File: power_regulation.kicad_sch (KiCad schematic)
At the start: 122 parts, among them IC3 NCV8184DR2G, IC4 MIE1W0505BGLVH-3R-P, J10 Conn_01x02_Pin, J7 V_bat_secondary, J8 Conn_01x02_Pin, J9 Conn_01x02_Pin, U10 OPA2387DR, U11 TPS7A2055PDBVR, U12 AP7361C-33Y5-13, U13 TPS7A2050PDBVR, U14 TPS7A2033PDBVR, U15 TPS7A2018PDBVRG4, U16 TLV75733PDYDR, U17 TPS7A2050PDBVR, U18 TPS7A2050PDBVR, U19 TPS7A2033PDBVR, U20 TPS7A2045PDBVR, U7 MCP1502T-50E/CHY, U8 TPS62933, U9 TPS62933

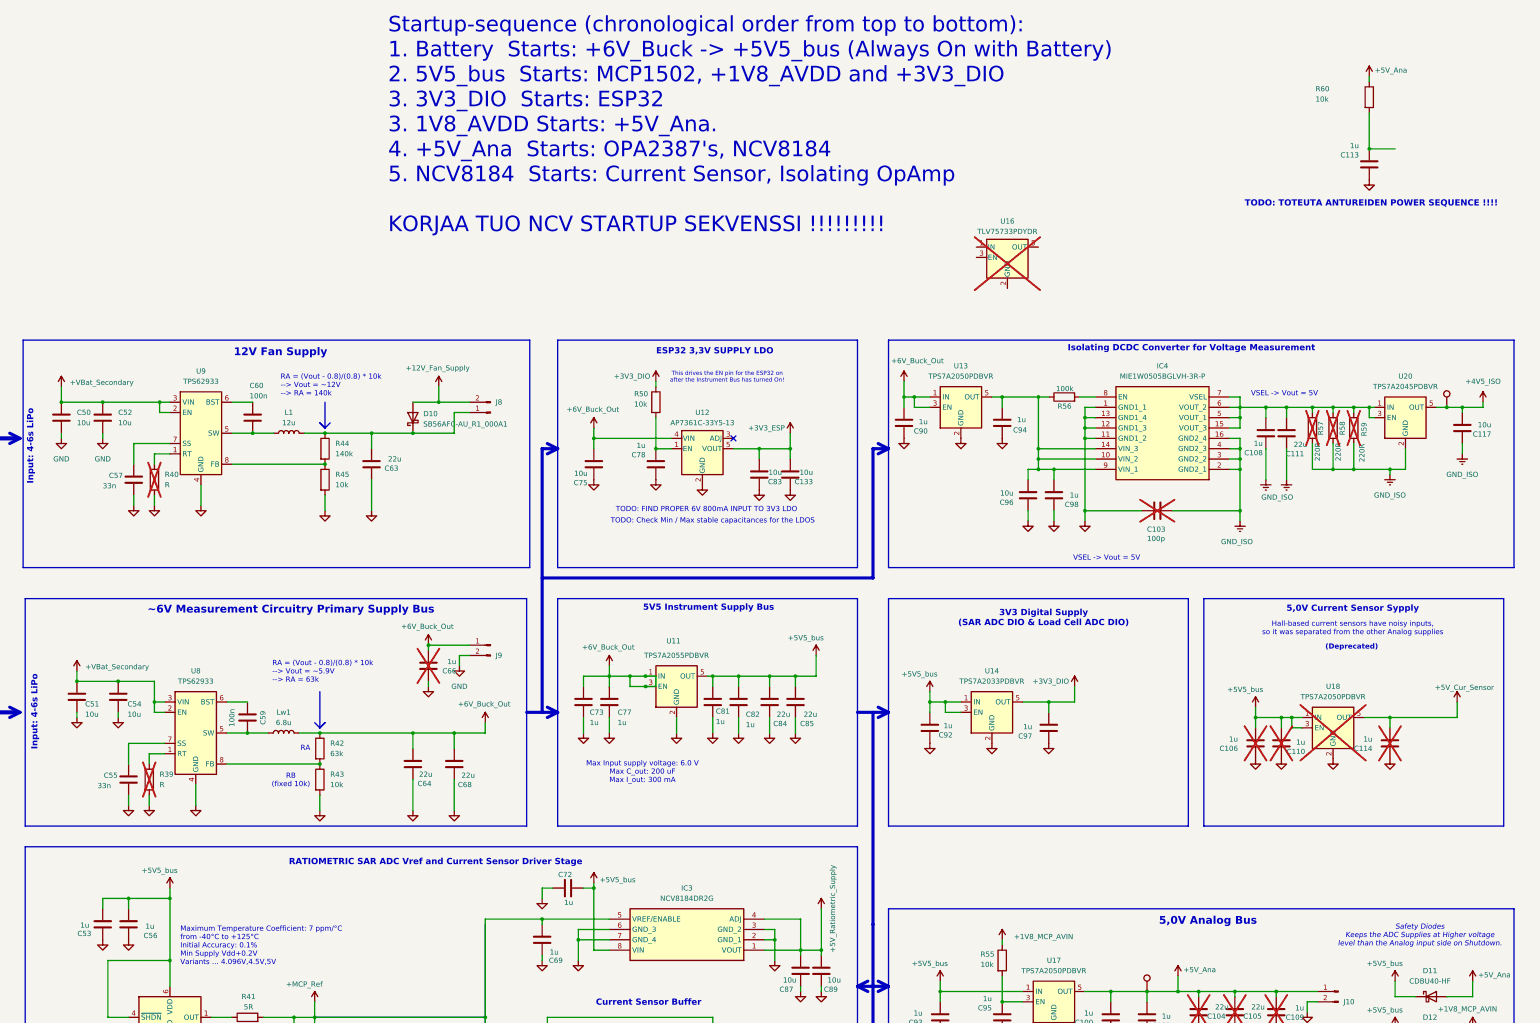
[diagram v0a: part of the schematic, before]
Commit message: Add LDO / Power sequencing for sensors
[KiCad Version: 10.0.3]
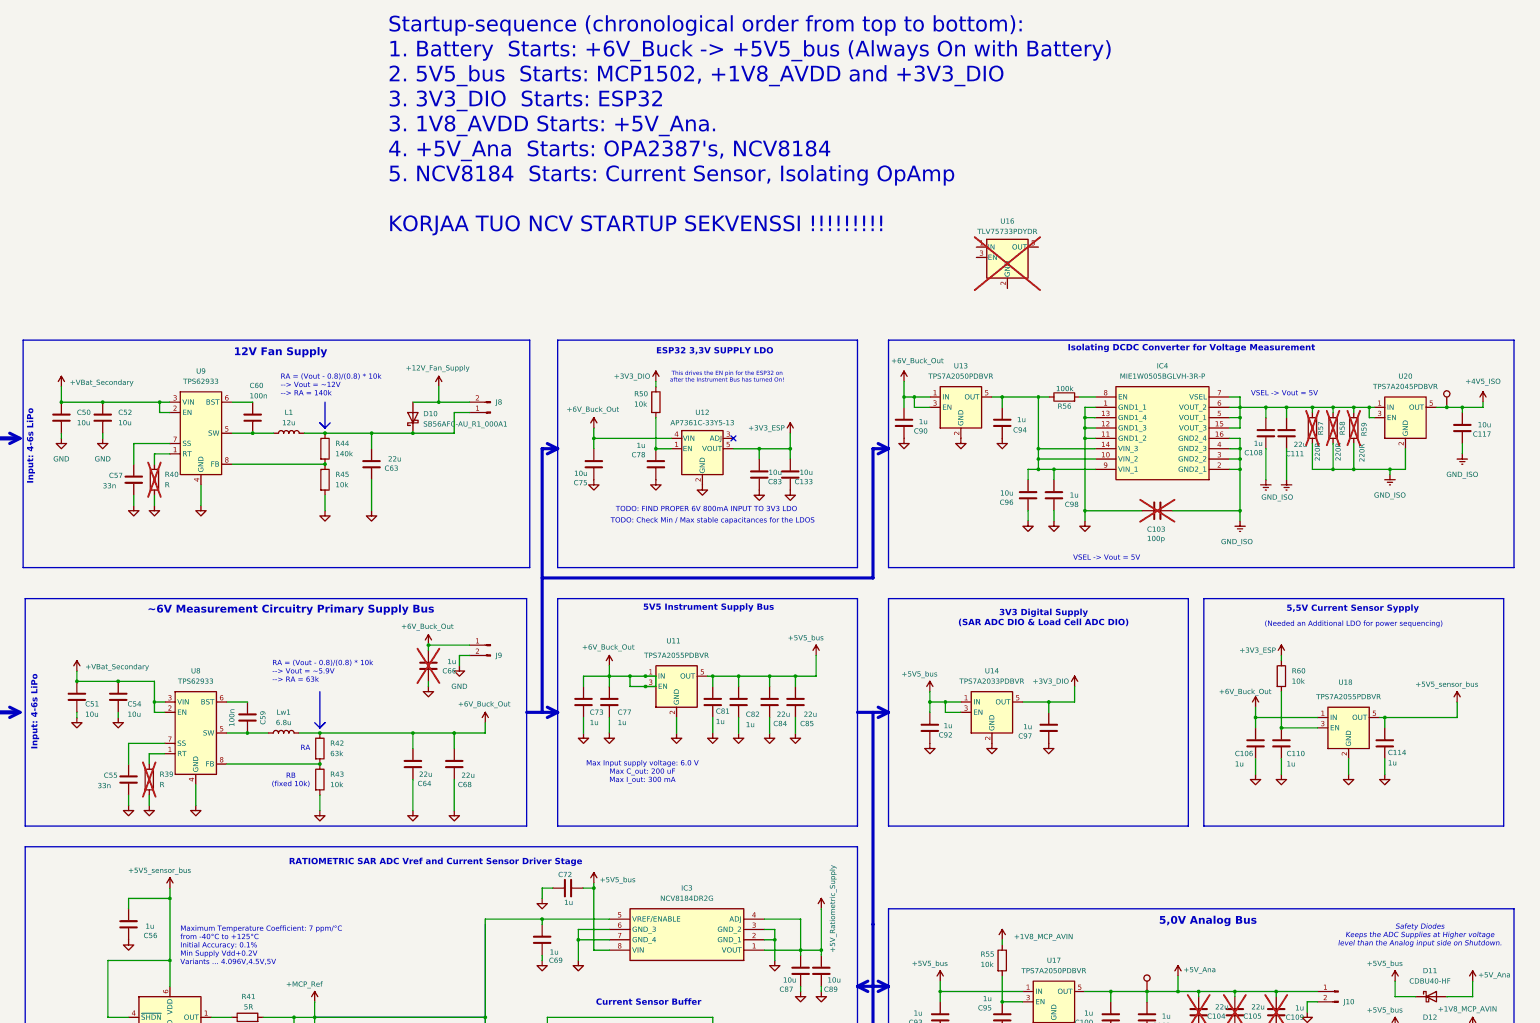
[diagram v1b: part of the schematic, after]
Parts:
- removed C113, C53: 1u, Capacitor_SMD:C_0603_1608Metric_Pad1.08x0.95mm_HandSolder, symbol Device:C
- C106, C110, C114: now fitted
- U18: value TPS7A2050PDBVR -> TPS7A2055PDBVR; Manufacturing_Number TPS7A2050PDBVR -> TPS7A2055PDBVR; Mouser_nro (none) -> 595-TPS7A2055PDBVR; now fitted
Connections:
- net +3V3_ESP: now also R60.1
- net +5V5_bus: no longer C106.2, C110.2, C56.2, U18.1 (IN), U18.3 (EN), U7.4 (~{SHDN}), U7.6 (VDD)
- net +5V_Ana: no longer R60.1
- net +6V_Buck_Out: now also C106.1, U18.1 (IN)
- net GND: now also C106.2, C110.2, C114.2; no longer C106.1, C110.1, C114.1
- net at R60.2: now also C110.1, U18.3 (EN)
- net +5V_Cur_Sensor renamed +5V5_sensor_bus
- net +5V5_sensor_bus: now also C114.1, C56.2, U7.4 (~{SHDN}), U7.6 (VDD); no longer C114.2
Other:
- note added: "(Needed an Additional LDO for power sequencing)"
- note added: "5,5V Current Sensor Sypply"
- note removed: "(Deprecated)"
- note removed: "5,0V Current Sensor Sypply"
- note removed: "Hall-based current sensors have noisy inputs, so it was separated from the other Analog supplies"
- note removed: "TODO: TOTEUTA ANTUREIDEN POWER SEQUENCE !!!!"

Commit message: Minor improvements
[KiCad Version: 10.0.3]
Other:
- note added: "Startup-sequence (chronological order from top to bottom): 1. Battery Starts: +6V_Buck -> +5V5_bus (Always On with Battery) 2. 5V5_bus Starts: MCP1502, +1V8_AVDD and +3V3_DIO 3.1 3V3_DIO Starts: ESP32 3.2 1V8_AVDD Starts: +5V_Ana. 4.1 3V3_ESP32 Starts: Sensors 4.2 +5V_Ana Starts: OPA2387's, NCV8184"
- note removed: "Startup-sequence (chronological order from top to bottom): 1. Battery Starts: +6V_Buck -> +5V5_bus (Always On with Battery) 2. 5V5_bus Starts: MCP1502, +1V8_AVDD and +3V3_DIO 3. 3V3_DIO Starts: ESP32 3. 1V8_AVDD Starts: +5V_Ana. 4. +5V_Ana Starts: OPA2387's, NCV8184 5. NCV8184 Starts: Current Sensor, Isolating OpAmp KORJAA TUO NCV STARTUP SEKVENSSI !!!!!!!!!"
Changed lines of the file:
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@@
 		)
 	)
-	(text "Startup-sequence (chronological order from top to bottom):\n1. Battery  Starts: +6V_Buck -> +5V5_bus (Always On with Battery) \n2. 5V5_bus  Starts: MCP1502, +1V8_AVDD and +3V3_DIO\n3. 3V3_DIO  Starts: ESP32\n3. 1V8_AVDD Starts: +5V_Ana.\n4. +5V_Ana  Starts: OPA2387's, NCV8184\n5. NCV8184  Starts: Current Sensor, Isolating OpAmp\n\nKORJAA TUO NCV STARTUP SEKVENSSI !!!!!!!!!"
+	(text "Startup-sequence (chronological order from top to bottom):\n1. Battery    Starts: +6V_Buck -> +5V5_bus (Always On with Battery) \n2. 5V5_bus    Starts: MCP1502, +1V8_AVDD and +3V3_DIO\n3.1 3V3_DIO   Starts: ESP32\n3.2 1V8_AVDD  Starts: +5V_Ana.\n4.1 3V3_ESP32 Starts: Sensors\n4.2 +5V_Ana   Starts: OPA2387's, NCV8184\n"
 		(exclude_from_sim no)
 		(at 124.714 -33.782 0)
@@
 	)
 	(junction
-		(at 187.96 101.6)
-		(diameter 0)
-		(color 0 0 0 0)
-	)
-	(junction
 		(at 162.56 161.29)
 		(diameter 0)
@@
 	)
 	(junction
-		(at 187.96 104.14)
-		(diameter 0)
-		(color 0 0 0 0)
-	)
-	(junction
 		(at 302.26 228.6)
 		(diameter 0)
@@
 	(wire
 		(pts
-			(xy 187.96 101.6) (xy 190.5 101.6)
-		)
-		(stroke
-			(width 0)
-			(type default)
-		)
-	)
-	(wire
-		(pts
 			(xy 62.23 57.15) (xy 62.23 59.69)
 		)
@@
 	(wire
 		(pts
-			(xy 190.5 101.6) (xy 190.5 104.14)
-		)
-		(stroke
-			(width 0)
-			(type default)
-		)
-	)
-	(wire
-		(pts
 			(xy 102.87 115.57) (xy 107.95 115.57)
 		)
@@
 		)
 		(stroke
-			(width 0)
-			(type default)
-		)
-	)
-	(wire
-		(pts
-			(xy 187.96 104.14) (xy 190.5 104.14)
-		)
-		(stroke

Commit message: Fix Via offset.
[KiCad Version: 10.0.4]
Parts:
- removed U12: AP7361C-33Y5-13, Package_TO_SOT_SMD:SOT-89-5_Handsoldering, symbol Regulator_Linear:AP7361C-33E
- removed U16: TLV75733PDYDR, Package_TO_SOT_SMD:SOT-23-5, symbol Regulator_Linear:TLV75733PDBV
- added IC4: AP7361C-33Y5-13, AP7361CY513, symbol SamacSys_Parts:AP7361C-33Y5-13
- renumbered C106 to C100, C107 to C101, C108 to C102, C109 to C103, C110 to C104, C111 to C105, C112 to C106, C114 to C107, C115 to C108, C116 to C109, C117 to C110, C50 to C44, C51 to C45, C52 to C46, C54 to C47, C55 to C48, C56 to C49, C57 to C50, C58 to C51, C59 to C52, C60 to C53, C61 to C54, C62 to C55, C63 to C56, C64 to C57, C65 to C58, C66 to C59, C67 to C60, C68 to C61, C69 to C62, C70 to C63, C71 to C64, C72 to C65, C73 to C66, C83 to C67, C74 to C68, C76 to C69, C77 to C70, C133 to C71, C79 to C72, C75 to C73, C80 to C74, C81 to C75, C82 to C76, C84 to C77, C85 to C78, C86 to C79, C87 to C80, C88 to C81, C89 to C82, C78 to C83, C90 to C84, C91 to C85, C92 to C86, C93 to C87, C94 to C88, C95 to C89, C96 to C90, C97 to C91, C98 to C92, C99 to C93, C100 to C94, C101 to C95, C102 to C96, C103 to C97, C104 to C98, C105 to C99, D12 to D10, D8 to D6, D9 to D7, D10 to D8, D11 to D9, IC4 to IC5, J7 to J5, J8 to J6, J9 to J7, J10 to J8, R39 to R40, R40 to R41, R41 to R42, R42 to R43, R43 to R44, R44 to R45, R45 to R46, R46 to R47, R47 to R48, R48 to R49, R49 to R50, R50 to R55, R55 to R56, R56 to R57, R60 to R58, R57 to R59, R58 to R60, R59 to R61, Vref1 to TP1, U13 to U12, U14 to U13, U15 to U14, U17 to U15, U18 to U16, U19 to U17, U20 to U18, Vref2 to Vref1
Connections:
- net +3V3_ESP: now also IC4.5 (OUT)
- net +6V_Buck_Out: now also IC4.4 (IN)
- net GND: now also IC4.2 (GND_1), IC4.6 (GND_2)
- net at C83.2, R55.2: now also IC4.1 (EN)
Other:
- moved on the sheet: C67, C71, C73, C83, R55

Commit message: Minor improvements. Fix capacitor sizes.
[KiCad Version: 10.0.4]
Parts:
- C100: renamed from C99; footprint Capacitor_SMD:C_1206_3216Metric_Pad1.33x1.80mm_HandSolder -> Capacitor_SMD:C_0805_2012Metric_Pad1.18x1.45mm_HandSolder
- C106: renamed from C105; footprint Capacitor_SMD:C_1206_3216Metric_Pad1.33x1.80mm_HandSolder -> Capacitor_SMD:C_0805_2012Metric_Pad1.18x1.45mm_HandSolder
- C111: renamed from C110; footprint Capacitor_SMD:C_0603_1608Metric_Pad1.08x0.95mm_HandSolder -> Capacitor_SMD:C_0805_2012Metric_Pad1.18x1.45mm_HandSolder
- C45: renamed from C44; footprint Capacitor_SMD:C_0603_1608Metric_Pad1.08x0.95mm_HandSolder -> Capacitor_SMD:C_0805_2012Metric_Pad1.18x1.45mm_HandSolder
- C46: renamed from C45; footprint Capacitor_SMD:C_0603_1608Metric_Pad1.08x0.95mm_HandSolder -> Capacitor_SMD:C_0805_2012Metric_Pad1.18x1.45mm_HandSolder
- C47: renamed from C46; footprint Capacitor_SMD:C_0603_1608Metric_Pad1.08x0.95mm_HandSolder -> Capacitor_SMD:C_0805_2012Metric_Pad1.18x1.45mm_HandSolder
- C48: renamed from C47; footprint Capacitor_SMD:C_0603_1608Metric_Pad1.08x0.95mm_HandSolder -> Capacitor_SMD:C_0805_2012Metric_Pad1.18x1.45mm_HandSolder
- C55: renamed from C54; footprint Capacitor_SMD:C_0603_1608Metric_Pad1.08x0.95mm_HandSolder -> Capacitor_SMD:C_0805_2012Metric_Pad1.18x1.45mm_HandSolder
- C56: renamed from C55; footprint Capacitor_SMD:C_0603_1608Metric_Pad1.08x0.95mm_HandSolder -> Capacitor_SMD:C_0805_2012Metric_Pad1.18x1.45mm_HandSolder
- C57: renamed from C56; footprint Capacitor_SMD:C_1206_3216Metric_Pad1.33x1.80mm_HandSolder -> Capacitor_SMD:C_0805_2012Metric_Pad1.18x1.45mm_HandSolder
- C58: renamed from C57; footprint Capacitor_SMD:C_1206_3216Metric_Pad1.33x1.80mm_HandSolder -> Capacitor_SMD:C_0805_2012Metric_Pad1.18x1.45mm_HandSolder
- C62: renamed from C61; footprint Capacitor_SMD:C_1206_3216Metric_Pad1.33x1.80mm_HandSolder -> Capacitor_SMD:C_0805_2012Metric_Pad1.18x1.45mm_HandSolder
- C68: renamed from C67; footprint Capacitor_SMD:C_0603_1608Metric_Pad1.08x0.95mm_HandSolder -> Capacitor_SMD:C_0805_2012Metric_Pad1.18x1.45mm_HandSolder
- C72: renamed from C71; footprint Capacitor_SMD:C_0603_1608Metric_Pad1.08x0.95mm_HandSolder -> Capacitor_SMD:C_0805_2012Metric_Pad1.18x1.45mm_HandSolder
- C78: renamed from C77; footprint Capacitor_SMD:C_1206_3216Metric_Pad1.33x1.80mm_HandSolder -> Capacitor_SMD:C_0805_2012Metric_Pad1.18x1.45mm_HandSolder
- C79: renamed from C78; footprint Capacitor_SMD:C_1206_3216Metric_Pad1.33x1.80mm_HandSolder -> Capacitor_SMD:C_0805_2012Metric_Pad1.18x1.45mm_HandSolder
- C81: renamed from C80; footprint Capacitor_SMD:C_0603_1608Metric_Pad1.08x0.95mm_HandSolder -> Capacitor_SMD:C_0805_2012Metric_Pad1.18x1.45mm_HandSolder
- C83: renamed from C82; footprint Capacitor_SMD:C_0603_1608Metric_Pad1.08x0.95mm_HandSolder -> Capacitor_SMD:C_0805_2012Metric_Pad1.18x1.45mm_HandSolder
- C91: renamed from C90; footprint Capacitor_SMD:C_0603_1608Metric_Pad1.08x0.95mm_HandSolder -> Capacitor_SMD:C_0805_2012Metric_Pad1.18x1.45mm_HandSolder
- C99: renamed from C98; footprint Capacitor_SMD:C_1206_3216Metric_Pad1.33x1.80mm_HandSolder -> Capacitor_SMD:C_0805_2012Metric_Pad1.18x1.45mm_HandSolder
- IC3: footprint SOIC127P600X175-8N -> SamacSys_Parts:SOIC127P600X175-8N
- IC4: footprint AP7361CY513 -> SamacSys_Parts:AP7361CY513
- IC5: footprint MIE1W0505BGLVH3RP -> SamacSys_Parts:MIE1W0505BGLVH3RP
- renumbered C100 to C101, C101 to C102, C102 to C103, C103 to C104, C104 to C105, C106 to C107, C107 to C108, C108 to C109, C109 to C110, C48 to C49, C49 to C50, C50 to C51, C51 to C52, C52 to C53, C53 to C54, C58 to C59, C59 to C60, C60 to C61, C62 to C63, C63 to C64, C64 to C65, C65 to C66, C66 to C67, C68 to C69, C69 to C70, C70 to C71, C72 to C73, C73 to C74, C74 to C75, C75 to C76, C76 to C77, C79 to C80, C81 to C82, C83 to C84, C84 to C85, C85 to C86, C86 to C87, C87 to C88, C88 to C89, C89 to C90, C91 to C92, C92 to C93, C93 to C94, C94 to C95, C95 to C96, C96 to C97, C97 to C98

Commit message: PCB improvements.
[KiCad Version: 10.0.4]
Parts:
- added C73: 10u, Capacitor_SMD:C_0805_2012Metric_Pad1.18x1.45mm_HandSolder, symbol Device:C
- renumbered C99 to C100, C100 to C101, C101 to C102, C102 to C103, C103 to C104, C104 to C105, C105 to C106, C106 to C107, C107 to C108, C108 to C109, C109 to C110, C110 to C111, C111 to C112, C73 to C74, C74 to C75, C75 to C76, C76 to C77, C77 to C78, C78 to C79, C79 to C80, C80 to C81, C81 to C82, C82 to C83, C83 to C84, C84 to C85, C85 to C86, C86 to C87, C87 to C88, C88 to C89, C89 to C90, C90 to C91, C91 to C92, C92 to C93, C93 to C94, C94 to C95, C95 to C96, C96 to C97, C97 to C98, C98 to C99, IN1 to IN3, TP1 to TP5
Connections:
- net +3V3_ESP: now also C73.2
- net GND: now also C73.1

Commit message: PCB Improvements.
[KiCad Version: 10.0.4]
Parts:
- renumbered IN3 to IN1, J8 to J10, J5 to J6, J6 to J7, J7 to J8, TP5 to TP8

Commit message: Add TPS7A20 LDO descriptions.
[KiCad Version: 10.0.4]
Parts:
- U13: Manufacturing_Number (none) -> TPS7A2033PDBVR
- U17: Manufacturer_Number (none) -> TPS7A2033PDBVR
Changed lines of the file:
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@@
 			)
 		)
-		(property "Description" "TPS7A2018PDBVRG4"
+		(property "Description" "LDO Voltage Regulators 300-mA ultra-low-noi se low-IQ low-dropo"
 			(at 275.59 231.14 0)
 			(hide yes)
@@
 			)
 		)
-		(property "Description" "TPS7A2045PDBVR"
+		(property "Description" "LDO Voltage Regulators 300-mA ultra-low-noi se low-IQ low-dropo"
 			(at 374.65 38.1 0)
 			(hide yes)
@@
 			)
 		)
-		(property "Description" "TPS7A2055PDBVR"
+		(property "Description" "LDO Voltage Regulators 300-mA ultra-low-noi se low-IQ low-dropo"
 			(at 195.58 104.14 0)
 			(hide yes)
@@
 			)
 		)
-		(property "Description" "TPS7A2055PDBVR"
+		(property "Description" "LDO Voltage Regulators 300-mA ultra-low-noi se low-IQ low-dropo"
 			(at 360.68 114.3 0)
 			(hide yes)
@@
 			)
 		)
-		(property "Description" "TPS7A2050PDBVR"
+		(property "Description" "LDO Voltage Regulators 300-mA ultra-low-noi se low-IQ low-dropo"
 			(at 288.29 181.61 0)
 			(hide yes)
@@
 			)
 		)
-		(property "Manufacturing_Number" ""
+		(property "Manufacturing_Number" "TPS7A2033PDBVR"
 			(at 273.05 110.49 0)
 			(hide yes)
@@
 			)
 		)
-		(property "Description" "TPS7A2033PDBVR"
+		(property "Description" "LDO Voltage Regulators 300-mA ultra-low-noi se low-IQ low-dropo"
 			(at 360.68 229.87 0)
 			(hide yes)
@@
 			)
 		)
-		(property "Manufacturing_Number" ""
+		(property "Manufacturer_Number" "TPS7A2033PDBVR"
 			(at 360.68 229.87 0)
 			(hide yes)
@@
 			)
 		)
-		(property "Description" "TPS7A2050PDBVR"
+		(property "Description" "LDO Voltage Regulators 300-mA ultra-low-noi se low-IQ low-dropo"
 			(at 265.43 35.56 0)
 			(hide yes)
